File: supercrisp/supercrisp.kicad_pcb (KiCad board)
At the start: 2 copper layers, 140 x 91 mm, 137 parts, among them J1 SWD, J2 SWD, SW1 SW_Push, SW10 SW_Push, SW11 SW_Push, SW12 SW_Push, SW13 SW_Push, SW14 SW_Push, SW15 SW_Push, SW16 SW_Push, SW17 SW_Push, SW18 SW_Push, SW19 SW_Push, SW2 SW_Push, SW20 SW_Push, SW21 SW_Push, SW22 SW_Push, SW23 SW_Push, SW24 SW_Push, SW25 SW_Push, SW26 SW_Push, SW27 SW_SPDT, SW28 SW_SPDT, SW3 SW_Push, SW4 SW_Push, SW5 SW_Push, SW6 SW_Push, SW7 SW_Push, SW8 SW_Push, SW9 SW_Push, U1 TPS82140, U4 TPS82140

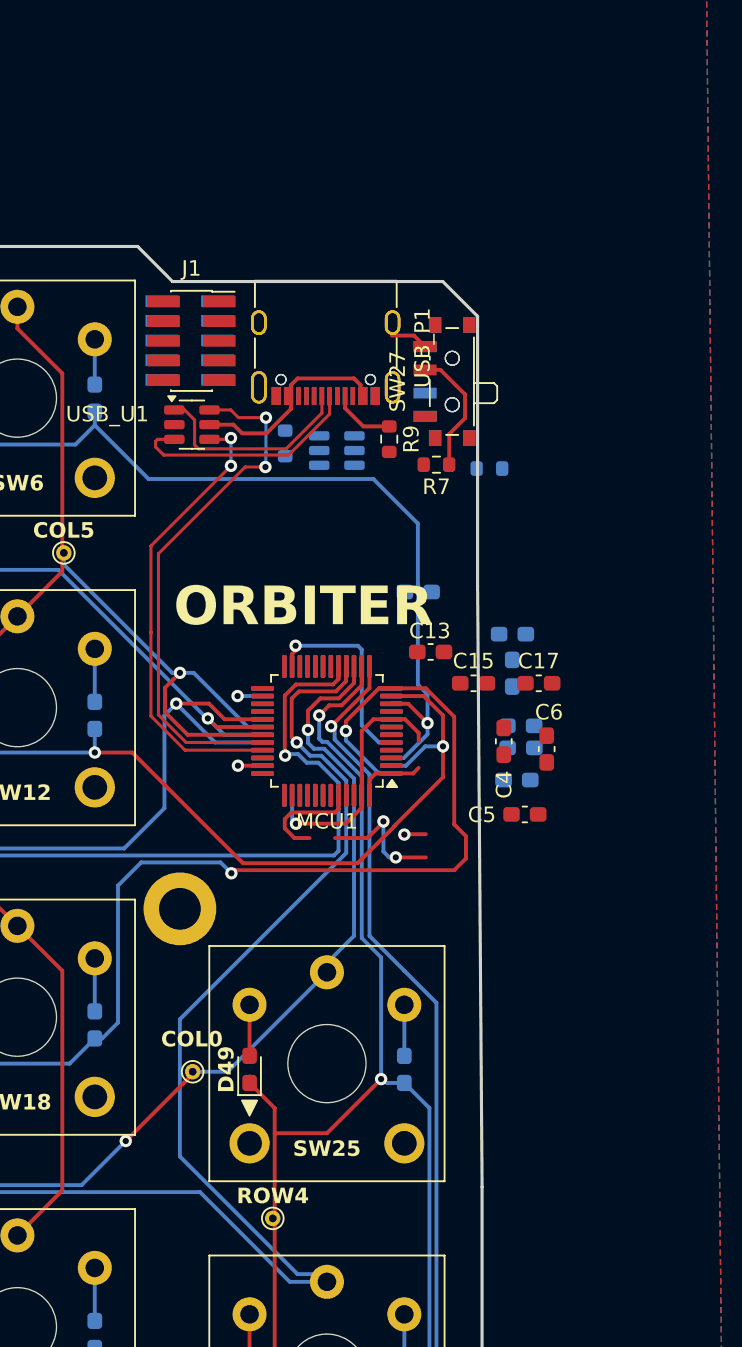
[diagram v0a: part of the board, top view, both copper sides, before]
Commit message: Add TRRS connector for serial communication between splits
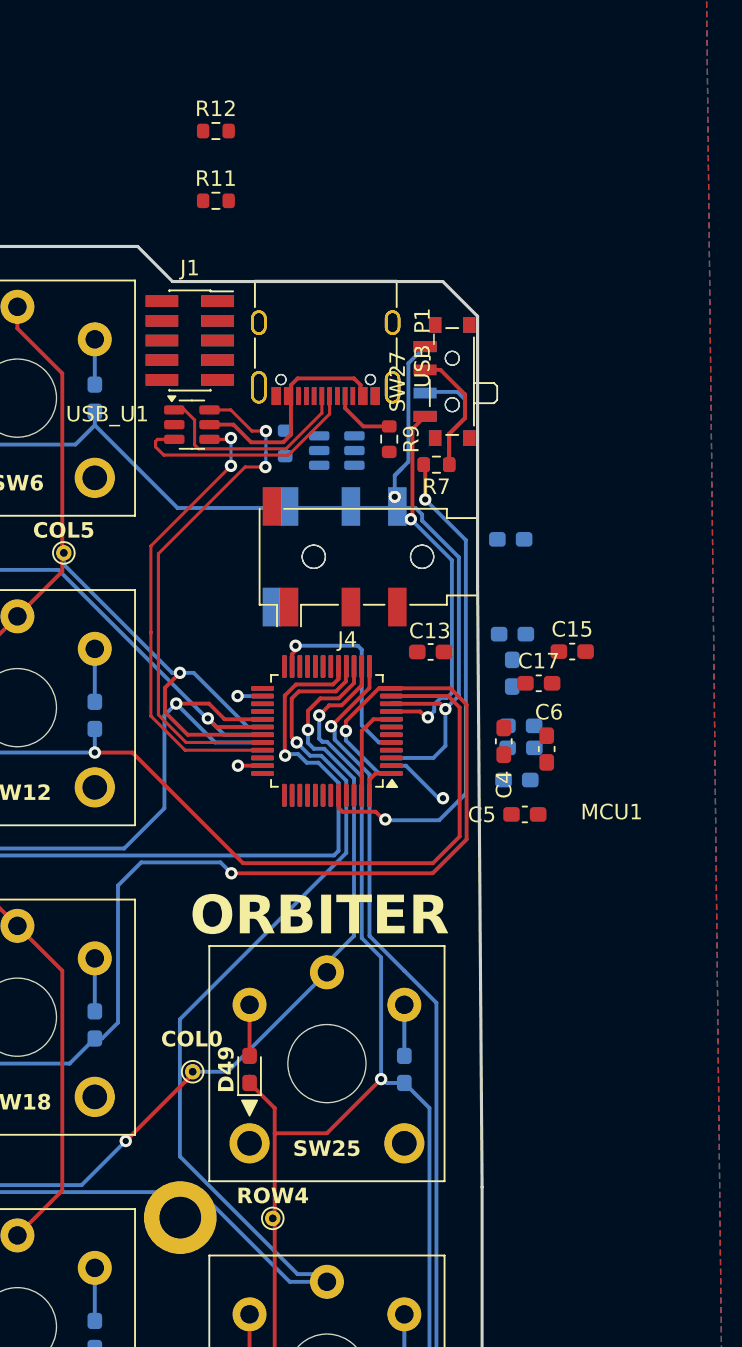
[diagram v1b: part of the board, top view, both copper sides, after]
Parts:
- added J4: AudioJack4, Connector_Audio:Jack_3.5mm_PJ320D_Horizontal, F.Cu at (201.4, 58.2)
- added J5: AudioJack4, Connector_Audio:Jack_3.5mm_PJ320D_Horizontal, B.Cu at (201.4, 58.2)
- added R11: 8.2k, Resistor_SMD:R_0603_1608Metric, F.Cu at (192.8, 35.2)
- added R12: 8.2k, Resistor_SMD:R_0603_1608Metric, F.Cu at (192.8, 30.7)
- moved G*** 20.1 mm to (198.6, 74.6)
- moved H6 20.0 mm to (190.5, 101.0)
- moved C18 6.87 mm to (211.9, 57.1)
- moved C15 6.70 mm to (215.8, 64.4)
- moved R8 3.43 mm to (207.1, 52.3)
- moved J1 0.10 mm to (191.2, 44.3)
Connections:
- MCU1 pad 21: unconnected-(MCU1-PB10-Pad21) -> /MCU_TOP/USART3_TX
- MCU2 pad 21: unconnected-(MCU2-PB10-Pad21) -> /MCU_BOTTOM/USART3_TX
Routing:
- net /MCU_TOP/BOOT0: track 7.09 -> 32.5 mm, vias 0 -> 2
- net /MCU_TOP/VOUT_3V3: track 10.9 -> 33.7 mm, vias 0 -> 2
- net GND: track 37.0 -> 22.7 mm, vias 5 -> 3
- net /MCU_BOTTOM/VOUT_3V3: track 0.00 -> 11.1 mm, vias 0 -> 1
- net Net-(SW27-B): track 16.9 -> 8.21 mm, vias 2 -> 0
- net Net-(SW28-B): track 0.00 -> 7.46 mm
- net /T_MCU_ROW1: track 171.6 -> 176.6 mm
- net /T_MCU_ROW0: track 174.5 -> 178.6 mm
- net /MCU_TOP/VBUS: track 13.5 -> 15.0 mm
- net /MCU_TOP/USB_D-: track 34.3 -> 33.8 mm

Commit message: Prel. placement of all components
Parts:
- R12: moved to B.Cu
- moved R12 33.1 mm to (193.5, 63.8), turned to 180 degrees
- moved R11 28.5 mm to (193.4, 63.8), turned to 180 degrees
- moved C16 22.6 mm to (193.1, 75.5), turned to -90 degrees
- moved C11 20.9 mm to (191.8, 71.7)
- moved C10 20.9 mm to (191.8, 73.2)
- moved C12 19.7 mm to (194.6, 74.9), turned to -90 degrees
- moved C14 16.4 mm to (196.1, 74.9), turned to -90 degrees
- moved C15 14.0 mm to (205.8, 74.0)
- moved C18 10.6 mm to (205.5, 65.6)
- moved C17 8.10 mm to (206.7, 70.5), turned to -90 degrees
- moved C4 7.76 mm to (205.8, 75.5), turned to 0 degrees
- moved C5 7.30 mm to (205.8, 77.0)
- moved C6 6.00 mm to (208.2, 70.5), turned to -90 degrees
- moved SW27 0.08 mm to (207.7, 46.9)
- moved U1 0.06 mm to (170.0, 73.8)
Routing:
- net /MCU_BOTTOM/VOUT_3V3: track 11.1 -> 24.2 mm
- net /MCU_TOP/VOUT_3V3: track 33.7 -> 42.4 mm
- net /MCU_TOP/USART3_TX: track 0.00 -> 8.53 mm
- net /T_MCU_ROW1: track 176.6 -> 180.3 mm
- net /T_MCU_ROW2: track 188.6 -> 191.4 mm
- net /MCU_TOP/BOOT0: track 32.5 -> 34.4 mm

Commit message: WIP 0 errors, 58 warnings
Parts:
- removed the C7 at (169.5, 64.4)
- removed the C8 at (171.3, 68.4)
- removed the C9 at (159.8, 74.7)
- removed the R2 at (165.8, 74.8)
- removed the R4 at (163.1, 74.2)
- removed the R6 at (173.5, 76.2)
- removed U4: TPS82140, Package_LGA:Texas_SIL0008D_MicroSiP-8-1EP_2.8x3mm_P0.65mm_EP1.1x1.9mm_ThermalVias
- removed USB_U2: USBLC6-2SC6, Package_TO_SOT_SMD:SOT-23-6
- added 3V3_TP1: TestPoint_Small, Testpoint_Rev:TestPoint_THTPad_D1.0mm_Drill0.5mm_reversible, F.Cu at (193.5, 65.6)
- added BOOT0_TP1: TestPoint_Small, Testpoint_Rev:TestPoint_THTPad_D1.0mm_Drill0.5mm_reversible, F.Cu at (205.6, 79.8)
- added NRST_TP1: TestPoint_Small, Testpoint_Rev:TestPoint_THTPad_D1.0mm_Drill0.5mm_reversible, F.Cu at (206.8, 61.6)
- added SWCLK_TP1: TestPoint_Small, Testpoint_Rev:TestPoint_THTPad_D1.0mm_Drill0.5mm_reversible, F.Cu at (199.9, 76.2)
- added SWDIO_TP1: TestPoint_Small, Testpoint_Rev:TestPoint_THTPad_D1.0mm_Drill0.5mm_reversible, F.Cu at (189.2, 63.4)
- added USART_TP1: TestPoint_Small, Testpoint_Rev:TestPoint_THTPad_D1.0mm_Drill0.5mm_reversible, F.Cu at (194.2, 56.2)
- added USB_CONN_DN_TP1: TestPoint_Small, Testpoint_Rev:TestPoint_THTPad_D1.0mm_Drill0.5mm_reversible, F.Cu at (200.3, 50.4)
- added USB_CONN_DP_TP1: TestPoint_Small, Testpoint_Rev:TestPoint_THTPad_D1.0mm_Drill0.5mm_reversible, F.Cu at (202.3, 51.7)
- added USB_DN_TP1: TestPoint_Small, Testpoint_Rev:TestPoint_THTPad_D1.0mm_Drill0.5mm_reversible, F.Cu at (192.2, 53.0)
- added USB_DP_TP1: TestPoint_Small, Testpoint_Rev:TestPoint_THTPad_D1.0mm_Drill0.5mm_reversible, F.Cu at (189.2, 52.5)
- added VBUS_TP1: TestPoint_Small, Testpoint_Rev:TestPoint_THTPad_D1.0mm_Drill0.5mm_reversible, F.Cu at (181.8, 78.3)
- U1: footprint Package_LGA:Texas_SIL0008D_MicroSiP-8-1EP_2.8x3mm_P0.65mm_EP1.1x1.9mm_ThermalVias -> Package_LGA:Texas_SIL0008D_MicroSiP-8-1EP_2.8x3mm_P0.65mm_EP1.1x1.9mm
- moved G*** 33.9 mm to (232.2, 70.1)
- moved C2 28.4 mm to (197.9, 79.1), turned to -90 degrees
- moved C3 24.6 mm to (190.3, 77.1), turned to -90 degrees
- moved C1 23.0 mm to (190.3, 73.8)
- moved U1 22.8 mm to (192.7, 75.5)
- moved R1 22.7 mm to (195.7, 78.2), turned to 0 degrees
- moved R3 22.7 mm to (193.4, 78.6), turned to -90 degrees
- moved R4 22.7 mm to (191.9, 78.6)
- moved C6 0.51 mm to (207.8, 70.8)
- moved C9 0.49 mm to (206.3, 70.8)
- moved COL2 0.25 mm to (103.0, 53.8)
- moved R11 0.08 mm to (193.4, 63.8)
- moved SW1 0.08 mm to (207.8, 46.9)
- turned USB_U1 to 180 degrees
- renumbered C10 to C13, C11 to C14, C12 to C15, C14 to C16, C16 to C17, C13 to C7, C15 to C8, C17 to C9, COL0 to COL1, COL1 to COL2, COL2 to COL3, COL3 to COL4, COL4 to COL5, COL5 to COL6, D50 to D10, D3 to D11, D15 to D12, D27 to D13, D39 to D14, D51 to D15, D4 to D16, D16 to D17, D28 to D18, D40 to D19, D13 to D2, D52 to D20, D5 to D21, D17 to D22, D29 to D23, D41 to D24, D6 to D25, D18 to D26, D30 to D27, D42 to D28, D7 to D29, D25 to D3, D19 to D30, D43 to D32, D8 to D33, D20 to D34, D32 to D35, D44 to D36, D9 to D37, D21 to D38, D33 to D39, D37 to D4, D45 to D40, D10 to D41, D22 to D42, D34 to D43, D46 to D44, D11 to D45, D23 to D46, D35 to D47, D47 to D48, D12 to D49, D49 to D5, D24 to D50, D36 to D51, D48 to D52, D2 to D6, D14 to D7, D26 to D8, D38 to D9, J4 to J2, J2 to J3, J5 to J4, R12 to R11, R8 to R12, R9 to R2, R5 to R4, R11 to R5, R7 to R6, R10 to R8, ROW0 to ROW1, ROW1 to ROW2, ROW2 to ROW3, ROW3 to ROW4, ROW4 to ROW5, SW27 to SW1, SW20 to SW10, SW26 to SW11, SW3 to SW12, SW9 to SW13, SW15 to SW14, SW21 to SW15, SW4 to SW16, SW10 to SW17, SW16 to SW18, SW22 to SW19, SW1 to SW2, SW5 to SW20, SW11 to SW21, SW17 to SW22, SW6 to SW24, SW12 to SW25, SW18 to SW26, SW24 to SW27, SW7 to SW3, SW13 to SW4, SW19 to SW5, SW25 to SW6, SW2 to SW7, SW14 to SW9
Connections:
- C1 pad 1: /MCU_TOP/VBUS -> /VBUS
- C13 pad 1: /MCU_BOTTOM/VOUT_3V3 -> /VOUT_3V3
- C14 pad 1: /MCU_BOTTOM/VOUT_3V3 -> /VOUT_3V3
- C15 pad 1: /MCU_BOTTOM/VOUT_3V3 -> /VOUT_3V3
- C16 pad 1: /MCU_BOTTOM/VOUT_3V3 -> /VOUT_3V3
- C17 pad 1: /MCU_BOTTOM/VOUT_3V3 -> /VOUT_3V3
- C18 pad 1: /MCU_BOTTOM/VOUT_3V3 -> /VOUT_3V3
- C3 pad 1: /MCU_TOP/VOUT_3V3 -> /VOUT_3V3
- C4 pad 1: /MCU_TOP/VOUT_3V3 -> /VOUT_3V3
- C5 pad 1: /MCU_TOP/VOUT_3V3 -> /VOUT_3V3
- C6 pad 1: /MCU_TOP/VOUT_3V3 -> /VOUT_3V3
- C7 pad 1: /MCU_TOP/VOUT_3V3 -> /VOUT_3V3
- C8 pad 1: /MCU_TOP/VOUT_3V3 -> /VOUT_3V3
- C9 pad 1: /MCU_TOP/VOUT_3V3 -> /VOUT_3V3
- J1 pad 1: /MCU_TOP/VOUT_3V3 -> /VOUT_3V3
- J1 pad 10: /MCU_TOP/NRST -> /NRST
- J1 pad 2: /MCU_TOP/SWDIO -> /SWDIO
- J1 pad 4: /MCU_TOP/SWCLK -> /SWCLK
- J2 pad R1: /MCU_TOP/USART3_TX -> /USART
- J2 pad R2: /MCU_TOP/USART3_TX -> /USART
- J2 pad T: /MCU_TOP/VOUT_3V3 -> /VOUT_3V3
- J3 pad 1: /MCU_BOTTOM/VOUT_3V3 -> /VOUT_3V3
- J3 pad 10: /MCU_BOTTOM/NRST -> /NRST
- J3 pad 2: /MCU_BOTTOM/SWDIO -> /SWDIO
- J3 pad 4: /MCU_BOTTOM/SWCLK -> /SWCLK
- J4 pad R1: /MCU_BOTTOM/USART3_TX -> /USART
- J4 pad R2: /MCU_BOTTOM/USART3_TX -> /USART
- J4 pad T: /MCU_BOTTOM/VOUT_3V3 -> /VOUT_3V3
- MCU1 pad 1: /MCU_TOP/VOUT_3V3 -> /VOUT_3V3
- MCU1 pad 21: /MCU_TOP/USART3_TX -> /USART
- MCU1 pad 24: /MCU_TOP/VOUT_3V3 -> /VOUT_3V3
- MCU1 pad 32: /MCU_TOP/USB_D- -> /USB_DN
- MCU1 pad 33: /MCU_TOP/USB_D+ -> /USB_DP
- MCU1 pad 34: /MCU_TOP/SWDIO -> /SWDIO
- MCU1 pad 36: /MCU_TOP/VOUT_3V3 -> /VOUT_3V3
- MCU1 pad 37: /MCU_TOP/SWCLK -> /SWCLK
- MCU1 pad 44: /MCU_TOP/BOOT0 -> /BOOT0
- MCU1 pad 48: /MCU_TOP/VOUT_3V3 -> /VOUT_3V3
- MCU1 pad 7: /MCU_TOP/NRST -> /NRST
- MCU1 pad 9: /MCU_TOP/VOUT_3V3 -> /VOUT_3V3
- MCU2 pad 1: /MCU_BOTTOM/VOUT_3V3 -> /VOUT_3V3
- MCU2 pad 21: /MCU_BOTTOM/USART3_TX -> /USART
- MCU2 pad 24: /MCU_BOTTOM/VOUT_3V3 -> /VOUT_3V3
- MCU2 pad 32: /MCU_BOTTOM/USB_D- -> /USB_DN
- MCU2 pad 33: /MCU_BOTTOM/USB_D+ -> /USB_DP
- MCU2 pad 34: /MCU_BOTTOM/SWDIO -> /SWDIO
- MCU2 pad 36: /MCU_BOTTOM/VOUT_3V3 -> /VOUT_3V3
- MCU2 pad 37: /MCU_BOTTOM/SWCLK -> /SWCLK
- MCU2 pad 44: /MCU_BOTTOM/BOOT0 -> /BOOT0
- MCU2 pad 48: /MCU_BOTTOM/VOUT_3V3 -> /VOUT_3V3
- MCU2 pad 7: /MCU_BOTTOM/NRST -> /NRST
- MCU2 pad 9: /MCU_BOTTOM/VOUT_3V3 -> /VOUT_3V3
- R1 pad 1: /MCU_TOP/VOUT_3V3 -> /VOUT_3V3
- R11 pad 1: /MCU_BOTTOM/USART3_TX -> /USART
- R11 pad 2: /MCU_BOTTOM/VOUT_3V3 -> /VOUT_3V3
- R12 pad 2: /MCU_BOTTOM/BOOT0 -> /BOOT0
- R3 pad 1: /MCU_TOP/VOUT_3V3 -> /VOUT_3V3
- R5 pad 1: /MCU_TOP/USART3_TX -> /USART
- R5 pad 2: /MCU_TOP/VOUT_3V3 -> /VOUT_3V3
- R6 pad 2: /MCU_TOP/BOOT0 -> /BOOT0
- SW1 pad 1: /MCU_TOP/VOUT_3V3 -> /VOUT_3V3
- SW28 pad 1: /MCU_BOTTOM/VOUT_3V3 -> /VOUT_3V3
- U1 pad 1: /MCU_TOP/VBUS -> /VBUS
- U1 pad 2: /MCU_TOP/VBUS -> /VBUS
- U1 pad 4: /MCU_TOP/VOUT_3V3 -> /VOUT_3V3
- U1 pad 5: /MCU_TOP/VOUT_3V3 -> /VOUT_3V3
- USB_P1 pad A4: /MCU_TOP/VBUS -> /VBUS
- USB_P1 pad A6: /MCU_TOP/USB_CONN_D+ -> /USB_CONN_DP
- USB_P1 pad A7: /MCU_TOP/USB_CONN_D- -> /USB_CONN_DN
- USB_P1 pad A9: /MCU_TOP/VBUS -> /VBUS
- USB_P1 pad B4: /MCU_TOP/VBUS -> /VBUS
- USB_P1 pad B9: /MCU_TOP/VBUS -> /VBUS
- USB_P2 pad A4: /MCU_BOTTOM/VBUS -> /VBUS
- USB_P2 pad A6: /MCU_BOTTOM/USB_CONN_D+ -> /USB_CONN_DP
- USB_P2 pad A7: /MCU_BOTTOM/USB_CONN_D- -> /USB_CONN_DN
- USB_P2 pad A9: /MCU_BOTTOM/VBUS -> /VBUS
- USB_P2 pad B4: /MCU_BOTTOM/VBUS -> /VBUS
- USB_P2 pad B9: /MCU_BOTTOM/VBUS -> /VBUS
- USB_U1 pad 1: /MCU_TOP/USB_CONN_D- -> /USB_CONN_DN
- USB_U1 pad 3: /MCU_TOP/USB_CONN_D+ -> /USB_CONN_DP
- USB_U1 pad 4: /MCU_TOP/USB_D+ -> /USB_DP
- USB_U1 pad 5: /MCU_TOP/VBUS -> /VBUS
- USB_U1 pad 6: /MCU_TOP/USB_D- -> /USB_DN
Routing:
- net /VOUT_3V3: track 0.00 -> 244.6 mm, vias 0 -> 10
- net GND: track 22.7 -> 193.7 mm, vias 3 -> 18
- net /SWCLK: track 0.00 -> 100.8 mm, vias 0 -> 7
- net /USART: track 0.00 -> 94.6 mm, vias 0 -> 5
- net /SWDIO: track 0.00 -> 77.7 mm, vias 0 -> 5
- net /VBUS: track 0.00 -> 75.5 mm, vias 0 -> 7
- net /BOOT0: track 0.00 -> 57.9 mm, vias 0 -> 3
- net /NRST: track 0.00 -> 53.4 mm, vias 0 -> 4
- net /USB_DP: track 0.00 -> 50.2 mm, vias 0 -> 3
- net /USB_DN: track 0.00 -> 44.4 mm, vias 0 -> 1
- net /MCU_TOP/VOUT_3V3: track 42.4 -> 0.00 mm, vias 2 -> 0
- net /MCU_TOP/BOOT0: track 34.4 -> 0.00 mm, vias 2 -> 0
- net /MCU_TOP/USB_D-: track 33.8 -> 0.00 mm, vias 2 -> 0
- net /USB_CONN_DP: track 0.00 -> 31.3 mm, vias 0 -> 1
- net /MCU_TOP/USB_D+: track 29.7 -> 0.00 mm, vias 2 -> 0
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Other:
- outline, holes or cut-outs redrawn

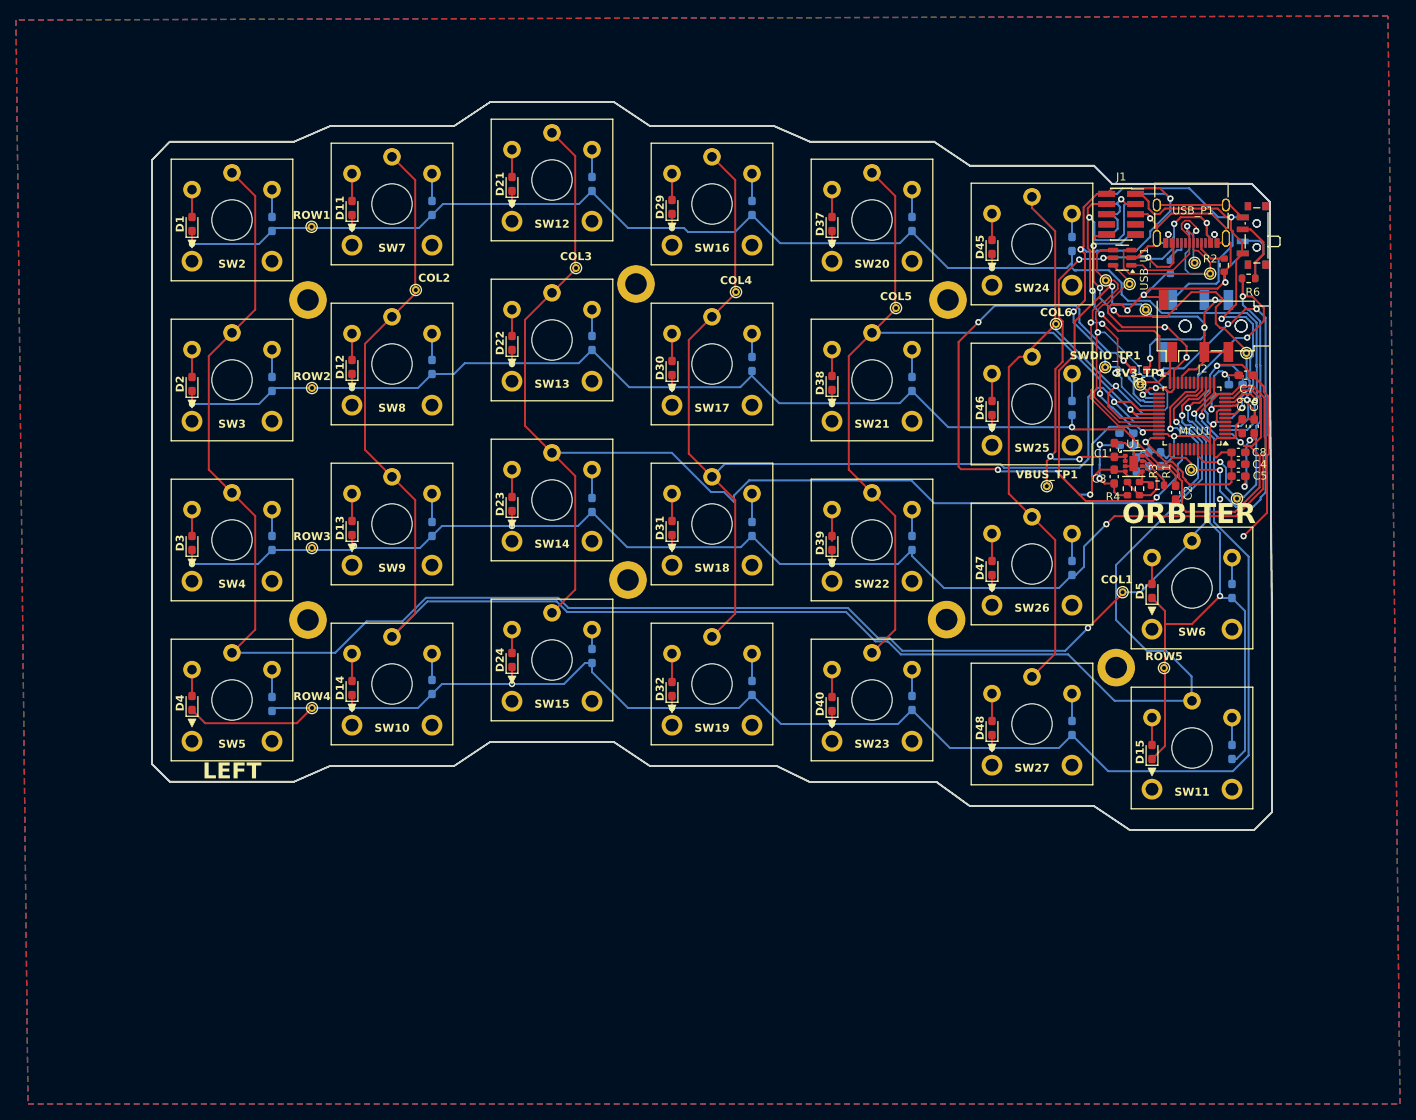
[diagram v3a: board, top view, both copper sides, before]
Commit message: Fix issue with duplicate edge cut
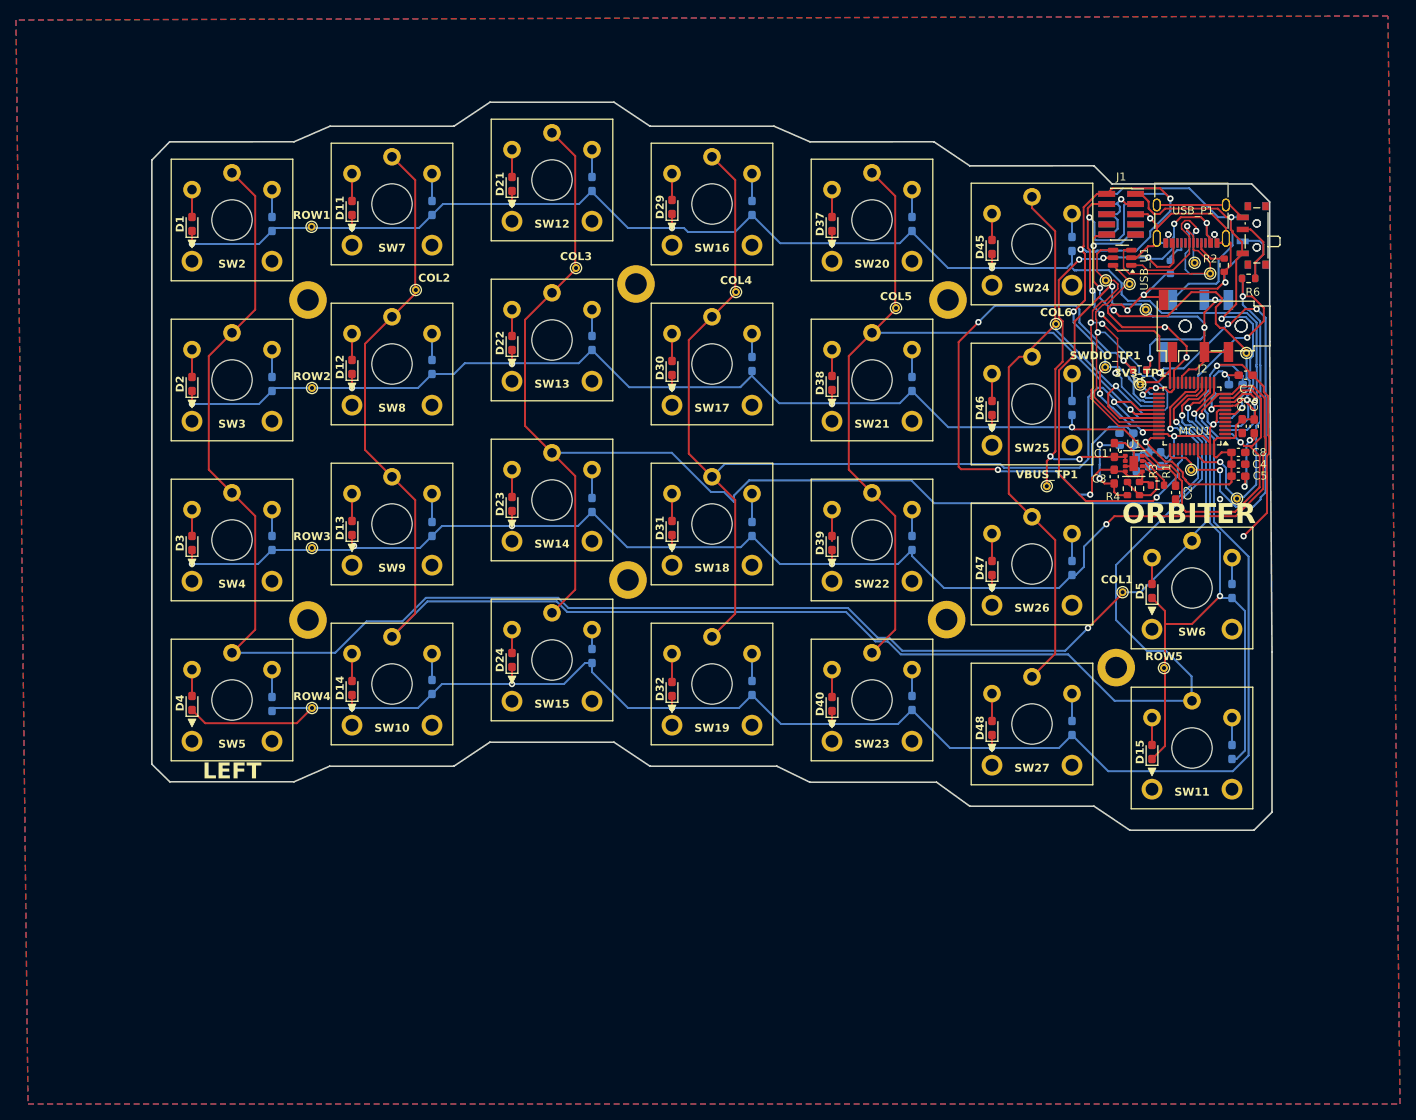
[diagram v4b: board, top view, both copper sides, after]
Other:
- outline, holes or cut-outs redrawn
